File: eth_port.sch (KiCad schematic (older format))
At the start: 49 parts, among them J301 8P8C_LED_Shielded, U201 LAN8831

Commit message: - Sanitized some of the capacitor voltages / footprints - Selected mfr P/Ns for *all* parts - Placed and routed most of the series resistors, ran into a problem with the   VDD vias on PHY1..... - Placed and routed (all?) the bypass caps for PHY2
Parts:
- C210: Part# (none) -> GCM21BR71A106KE22L; Voltage 6.3V -> 10V
- C311: footprint Capacitor_SMD:C_0603_1608Metric -> Capacitor_SMD:C_0805_2012Metric; Part# (none) -> GCM21BR71A106KE22L
- C319, C329: footprint Capacitor_SMD:C_0603_1608Metric -> Capacitor_SMD:C_0805_2012Metric; Part# (none) -> CGA4J1X7R0J106K125AC; Voltage 10V -> 6.3V
- C330: Part# (none) -> CGA2B2X7R1E103K050BA; Voltage 10V -> 6.3V
- C332: footprint Capacitor_SMD:C_0603_1608Metric -> Capacitor_SMD:C_0805_2012Metric; Part# (none) -> CGA4J3X7R1C475M125AB; Voltage 10V -> 6.3V
- U201: Part# (none) -> LAN8831-V/Q2A
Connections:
- net labels added: LDO_O
- net labels removed: VDDVARIO
- wire segments 213 -> 214
- no-connect marks 5 -> 6
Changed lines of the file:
@@
 F 0 "C219" H 6850 7200 50  0000 L CNN
 F 1 "10u" H 6850 7000 50  0000 L CNN
-F 2 "Capacitor_SMD:C_0603_1608Metric" H 6838 6950 50  0001 C CNN
+F 2 "Capacitor_SMD:C_0805_2012Metric" H 6838 6950 50  0001 C CNN
 F 3 "~" H 6800 7100 50  0001 C CNN
-F 4 "10V" H 6800 7100 50  0001 C CNN "Voltage"
+F 4 "6.3V" H 6800 7100 50  0001 C CNN "Voltage"
+F 5 "CGA4J1X7R0J106K125AC" H 0   0   50  0001 C CNN "Part#"
 	1    6800 7100
 	1    0    0    -1
@@
 F 0 "C229" H 6850 7700 50  0000 L CNN
 F 1 "10u" H 6850 7500 50  0000 L CNN
-F 2 "Capacitor_SMD:C_0603_1608Metric" H 6838 7450 50  0001 C CNN
+F 2 "Capacitor_SMD:C_0805_2012Metric" H 6838 7450 50  0001 C CNN
 F 3 "~" H 6800 7600 50  0001 C CNN
-F 4 "10V" H 6800 7600 50  0001 C CNN "Voltage"
+F 4 "6.3V" H 6800 7600 50  0001 C CNN "Voltage"
+F 5 "CGA4J1X7R0J106K125AC" H 0   0   50  0001 C CNN "Part#"
 	1    6800 7600
 	1    0    0    -1
@@
 	3550 1800 3800 1800
 Wire Wire Line
-	2950 1700 2550 1700
-Text Label 2550 1700 0    50   ~ 0
-VDDVARIO
+	2950 1700 2650 1700
+Text Label 2650 1700 0    50   ~ 0
+VDDIO
 Text Label 3550 1700 0    50   ~ 0
 MDIO
@@
 	6250 4800 6250 4750
 Wire Wire Line
-	5200 4800 6250 4800
-Wire Wire Line
 	6250 4800 6450 4800
 Wire Wire Line
@@
 F 2 "Capacitor_SMD:C_0805_2012Metric" H 6488 4850 50  0001 C CNN
 F 3 "~" H 6450 5000 50  0001 C CNN
-F 4 "6.3V" H 6565 4909 50  0000 L CNN "Voltage"
+F 4 "10V" H 6565 4909 50  0000 L CNN "Voltage"
+F 5 "GCM21BR71A106KE22L" H 0   0   50  0001 C CNN "Part#"
 	1    6450 5000
 	1    0    0    -1
@@
 F 2 "myfp:QFN-64-1EP_8x8mm_P0.4mm_EP6x6mm_ThermalVias" H 4500 1550 50  0001 C CNN
 F 3 "" H 4500 3250 50  0001 C CNN
+F 4 "LAN8831-V/Q2A" H 0   0   50  0001 C CNN "Part#"
 	1    4500 3250
 	1    0    0    -1
@@
 F 2 "myfp:QFN-64-1EP_8x8mm_P0.4mm_EP6x6mm_ThermalVias" H 4500 5850 50  0001 C CNN
 F 3 "" H 4500 7550 50  0001 C CNN
+F 4 "LAN8831-V/Q2A" H 0   0   50  0001 C CNN "Part#"
 	2    4500 7550
 	1    0    0    -1
@@
 F 2 "Capacitor_SMD:C_0402_1005Metric" H 5538 7950 50  0001 C CNN
 F 3 "~" H 5500 8100 50  0001 C CNN
-F 4 "10V" H 5500 8100 50  0001 C CNN "Voltage"
+F 4 "6.3V" H 5500 8100 50  0001 C CNN "Voltage"
+F 5 "CGA2B2X7R1E103K050BA" H 0   0   50  0001 C CNN "Part#"
 	1    5500 8100
 	1    0    0    -1
@@
 F 0 "C232" H 6150 8200 50  0000 L CNN
 F 1 "4.7u" H 6150 8000 50  0000 L CNN
-F 2 "Capacitor_SMD:C_0603_1608Metric" H 6138 7950 50  0001 C CNN
+F 2 "Capacitor_SMD:C_0805_2012Metric" H 6138 7950 50  0001 C CNN
 F 3 "~" H 6100 8100 50  0001 C CNN
-F 4 "10V" H 6100 8100 50  0001 C CNN "Voltage"
+F 4 "6.3V" H 6100 8100 50  0001 C CNN "Voltage"
+F 5 "CGA4J3X7R1C475M125AB" H 0   0   50  0001 C CNN "Part#"
 	1    6100 8100
 	1    0    0    -1
@@
 F 0 "C211" H 2250 7200 50  0000 L CNN
 F 1 "10u" H 2250 7000 50  0000 L CNN
-F 2 "Capacitor_SMD:C_0603_1608Metric" H 2238 6950 50  0001 C CNN
+F 2 "Capacitor_SMD:C_0805_2012Metric" H 2238 6950 50  0001 C CNN
 F 3 "~" H 2200 7100 50  0001 C CNN
 F 4 "10V" H 2200 7100 50  0001 C CNN "Voltage"
+F 5 "GCM21BR71A106KE22L" H 0   0   50  0001 C CNN "Part#"
 	1    2200 7100
 	1    0    0    -1
@@
 Wire Wire Line
 	7700 3550 7700 3000
-Wire Bus Line
-	3200 3250 3200 3950
-Wire Bus Line
-	3200 1900 3200 2600
 Text Label 7400 1600 0    50   ~ 0
 ETH_CR3
@@
 Text Label 7700 3450 1    50   ~ 0
 ETH_CR0
+Wire Wire Line
+	5200 4800 6250 4800
+Wire Wire Line
+	5100 8150 5200 8150
+NoConn ~ 5200 8150
+Text Label 5150 8150 0    50   ~ 0
+LDO_O
+Wire Bus Line
+	3200 3250 3200 3950
+Wire Bus Line
+	3200 1900 3200 2600
 $EndSCHEMATC

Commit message: Added the absurd number of config/MODE/PHYAD strap resistors, 16 per PHY !!! They have been added to the layout, but not yet placed or routed.
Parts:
- added R209, R210, R211, R212, R213, R214, R215, R216, R218, R219, R220, R221, R222, R223, R224: 10k, Resistor_SMD:R_0402_1005Metric, symbol Device:R_US
- added R217: dnp, Resistor_SMD:R_0402_1005Metric, symbol Device:R_US
- R202, R203: value 100 -> 220
- renumbered R209 to R225
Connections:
- net labels removed: 1000_LED, 100_LED
- wire segments 214 -> 274
- no-connect marks 6 -> 5
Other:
- note added: "CLK125_EN"
- note added: "CONFIG STRAPS"
- note added: "LED1 / right / yellow / 100bTx"
- note added: "LED2 / left / green / 1000bT"
- note added: "LED_MODE"
- note added: "MAGJACK"
- note added: "MODE[4..0]\n11000=10/100/1000 w/EEE"
- note added: "PHYAD[4..0]\nALLPHYAD"
- note added: "RGMII"
- note removed: "LED1 / right / yellow"
- note removed: "LED2 / left / green"
- moved on the sheet: R202, R203

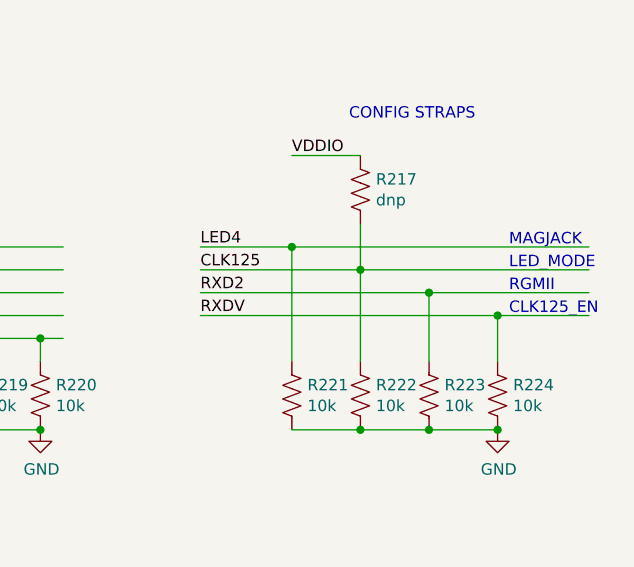
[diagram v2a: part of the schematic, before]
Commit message: - Fixed a schematic bug, one of the strap resistors was connected to RXD2 but   should have been RXD4 - Swapped out reset 10k resistor from size 0603 to size 0402, since I have now   32 more of them in the smaller size... also assigned a mfr P/N to all those - Placed and routed *EVERYTHING* for PHY2, mainly all the new strap resistors - Placed and routed the new LED traces (both PHYs), and a few of the PHY1   straps, namely the LED1-5 straps
Still to go: place & route of the config & PHYAD strap resistors for PHY1...
It's getting very crowded
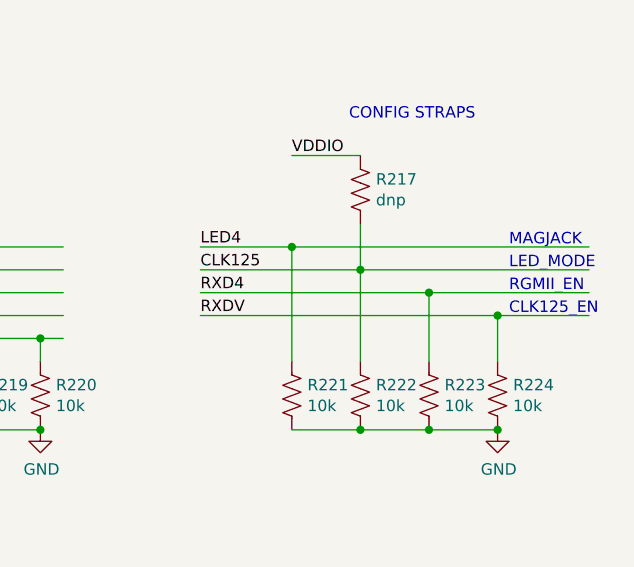
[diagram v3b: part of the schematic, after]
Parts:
- R208: footprint Resistor_SMD:R_0603_1608Metric -> Resistor_SMD:R_0402_1005Metric; Part# ERJ-3EKF1002V -> ERJ-2RKF1002X
- R209, R210, R211, R212, R213, R214, R215, R216, R218, R219, R220, R221, R222, R223, R224: Part# (none) -> ERJ-2RKF1002X
- R217: Part# (none) -> dnp
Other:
- note added: "RGMII_EN"
- note removed: "RGMII"
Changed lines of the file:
@@
 F 0 "R208" H 6318 4646 50  0000 L CNN
 F 1 "10k" H 6318 4555 50  0000 L CNN
-F 2 "Resistor_SMD:R_0603_1608Metric" V 6290 4590 50  0001 C CNN
+F 2 "Resistor_SMD:R_0402_1005Metric" V 6290 4590 50  0001 C CNN
 F 3 "~" H 6250 4600 50  0001 C CNN
-F 4 "ERJ-3EKF1002V" H 0   0   50  0001 C CNN "Part#"
+F 4 "ERJ-2RKF1002X" H 0   0   50  0001 C CNN "Part#"
 	1    6250 4600
 	1    0    0    -1
@@
 F 2 "Resistor_SMD:R_0402_1005Metric" V 12040 5740 50  0001 C CNN
 F 3 "~" H 12000 5750 50  0001 C CNN
+F 4 "ERJ-2RKF1002X" H 0   0   50  0001 C CNN "Part#"
 	1    12000 5750
 	1    0    0    -1
@@
 F 2 "Resistor_SMD:R_0402_1005Metric" V 12340 5740 50  0001 C CNN
 F 3 "~" H 12300 5750 50  0001 C CNN
+F 4 "ERJ-2RKF1002X" H 0   0   50  0001 C CNN "Part#"
 	1    12300 5750
 	1    0    0    -1
@@
 F 2 "Resistor_SMD:R_0402_1005Metric" V 12640 6640 50  0001 C CNN
 F 3 "~" H 12600 6650 50  0001 C CNN
+F 4 "ERJ-2RKF1002X" H 0   0   50  0001 C CNN "Part#"
 	1    12600 6650
 	1    0    0    -1
@@
 F 2 "Resistor_SMD:R_0402_1005Metric" V 12940 6640 50  0001 C CNN
 F 3 "~" H 12900 6650 50  0001 C CNN
+F 4 "ERJ-2RKF1002X" H 0   0   50  0001 C CNN "Part#"
 	1    12900 6650
 	1    0    0    -1
@@
 F 2 "Resistor_SMD:R_0402_1005Metric" V 13240 6640 50  0001 C CNN
 F 3 "~" H 13200 6650 50  0001 C CNN
+F 4 "ERJ-2RKF1002X" H 0   0   50  0001 C CNN "Part#"
 	1    13200 6650
 	1    0    0    -1
@@
 F 2 "Resistor_SMD:R_0402_1005Metric" V 9740 5740 50  0001 C CNN
 F 3 "~" H 9700 5750 50  0001 C CNN
+F 4 "ERJ-2RKF1002X" H 0   0   50  0001 C CNN "Part#"
 	1    9700 5750
 	1    0    0    -1
@@
 F 2 "Resistor_SMD:R_0402_1005Metric" V 10040 5740 50  0001 C CNN
 F 3 "~" H 10000 5750 50  0001 C CNN
+F 4 "ERJ-2RKF1002X" H 0   0   50  0001 C CNN "Part#"
 	1    10000 5750
 	1    0    0    -1
@@
 F 2 "Resistor_SMD:R_0402_1005Metric" V 10340 5740 50  0001 C CNN
 F 3 "~" H 10300 5750 50  0001 C CNN
+F 4 "ERJ-2RKF1002X" H 0   0   50  0001 C CNN "Part#"
 	1    10300 5750
 	1    0    0    -1
@@
 F 2 "Resistor_SMD:R_0402_1005Metric" V 10640 5740 50  0001 C CNN
 F 3 "~" H 10600 5750 50  0001 C CNN
+F 4 "ERJ-2RKF1002X" H 0   0   50  0001 C CNN "Part#"
 	1    10600 5750
 	1    0    0    -1
@@
 F 2 "Resistor_SMD:R_0402_1005Metric" V 10940 5740 50  0001 C CNN
 F 3 "~" H 10900 5750 50  0001 C CNN
+F 4 "ERJ-2RKF1002X" H 0   0   50  0001 C CNN "Part#"
 	1    10900 5750
 	1    0    0    -1
@@
 F 2 "Resistor_SMD:R_0402_1005Metric" V 11240 5740 50  0001 C CNN
 F 3 "~" H 11200 5750 50  0001 C CNN
+F 4 "ERJ-2RKF1002X" H 0   0   50  0001 C CNN "Part#"
 	1    11200 5750
 	1    0    0    -1
@@
 	13900 6200 14900 6200
 Text Label 13900 6200 0    50   ~ 0
-RXD2
+RXD4
 Wire Wire Line
 	13900 6300 15200 6300
@@
 F 2 "Resistor_SMD:R_0402_1005Metric" V 14340 6640 50  0001 C CNN
 F 3 "~" H 14300 6650 50  0001 C CNN
+F 4 "ERJ-2RKF1002X" H 0   0   50  0001 C CNN "Part#"
 	1    14300 6650
 	1    0    0    -1
@@
 F 2 "Resistor_SMD:R_0402_1005Metric" V 14640 5740 50  0001 C CNN
 F 3 "~" H 14600 5750 50  0001 C CNN
+F 4 "dnp" H 0   0   50  0001 C CNN "Part#"
 	1    14600 5750
 	1    0    0    -1
@@
 F 2 "Resistor_SMD:R_0402_1005Metric" V 14940 6640 50  0001 C CNN
 F 3 "~" H 14900 6650 50  0001 C CNN
+F 4 "ERJ-2RKF1002X" H 0   0   50  0001 C CNN "Part#"
 	1    14900 6650
 	1    0    0    -1
@@
 F 2 "Resistor_SMD:R_0402_1005Metric" V 15240 6640 50  0001 C CNN
 F 3 "~" H 15200 6650 50  0001 C CNN
+F 4 "ERJ-2RKF1002X" H 0   0   50  0001 C CNN "Part#"
 	1    15200 6650
 	1    0    0    -1
@@
 LED_MODE
 Text Notes 15250 6200 0    50   ~ 0
-RGMII
+RGMII_EN
 Text Notes 15250 6300 0    50   ~ 0
 CLK125_EN
@@
 F 2 "Resistor_SMD:R_0402_1005Metric" V 14640 6640 50  0001 C CNN
 F 3 "~" H 14600 6650 50  0001 C CNN
+F 4 "ERJ-2RKF1002X" H 0   0   50  0001 C CNN "Part#"
 	1    14600 6650
 	1    0    0    -1
